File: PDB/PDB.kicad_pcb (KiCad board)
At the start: 2 copper layers, 111.8 x 88.1 mm, 45 parts, among them J1 Conn_01x02, J2 Conn_01x04, Q1 S8050, Sw1 D-SWITCH_MR5-111-C5N-BB, Y1 12MHz

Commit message: Finished board layout?
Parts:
- added ?: , , F.Cu at (92.0, 102.0)
- added ?: , , F.Cu at (151.0, 102.0)
- added ?: , , F.Cu at (93.5, 53.2)
- added ?: , , F.Cu at (151.0, 60.0)
- added C7: 0.1u, Capacitor_SMD:C_0603_1608Metric, F.Cu at (137.2, 70.6)
- added G***: LOGO, PiE_Footprints:PiE Logo, F.Cu at (91.0, 51.5)
- added R17: 22, Resistor_SMD:R_0603_1608Metric, F.Cu at (153.9, 88.5)
- added R18: 22, Resistor_SMD:R_0603_1608Metric, F.Cu at (153.8, 86.5)
- added SW2: SW_SPDT, PiE_Footprints:DEALON SS-12D01-G3, F.Cu at (162.9, 100.9)
- added U3: PCF8574, PiE_Footprints:PCF8574T, F.Cu at (133.3, 76.9)
- Batt1: footprint PiE_Footprints:XT60_F -> PiE_Footprints:AMASS_XT60-M_1x02_P7.20mm_Vertical
- J1: footprint Connector_PinHeader_2.54mm:PinHeader_1x02_P2.54mm_Vertical -> PiE_Footprints:PinHeader_1x02_P2.54mm_Vertical
- J2: footprint Connector_PinHeader_2.54mm:PinHeader_1x04_P2.54mm_Vertical -> PiE_Footprints:PinHeader_1x04_P2.54mm_Vertical
- Jst1: footprint PiE_Footprints:JST_XH_B4B-XH-AM_1x04_P2.50mm_Vertical -> PiE_Footprints:JST_XH_B4B-XH-A_1x04_P2.50mm_Vertical
- Y1: footprint Crystal:Crystal_HC49-U_Vertical -> PiE_Footprints:JYJE S1C12000VWFAC
- moved J2 53.4 mm to (78.5, 101.6), turned to 180 degrees
- moved R1 40.7 mm to (93.6, 95.5), turned to 90 degrees
- moved R2 36.5 mm to (93.6, 92.4), turned to 90 degrees
- moved Pro1 28.2 mm to (104.1, 87.1)
- moved R4 27.2 mm to (93.6, 87.8), turned to 90 degrees
- moved C1 26.2 mm to (122.5, 72.4)
- moved R14 26.0 mm to (137.2, 86.5)
- moved R3 25.9 mm to (93.6, 84.6), turned to -90 degrees
- moved D3 25.4 mm to (130.8, 96.3)
- moved R13 24.3 mm to (127.6, 86.5)
- moved R9 24.3 mm to (122.2, 86.5)
- moved R12 24.3 mm to (126.0, 86.5)
- moved R7 24.3 mm to (118.9, 86.5)
- moved R8 24.3 mm to (120.5, 86.5)
- moved R10 22.1 mm to (138.9, 86.5)
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- renumbered USB4 to DATA1, FTDI1 to U2
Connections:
- DATA1 pad 2: /D- -> Net-(DATA1-Pad2)
- DATA1 pad 3: /D+ -> Net-(DATA1-Pad3)
- Pro1 pad 10: /E -> unconnected-(Pro1-Pad10)
- Pro1 pad 11: /DP -> unconnected-(Pro1-Pad11)
- Pro1 pad 12: /Buzzer -> /Dig4
- Pro1 pad 13: /A -> /Buzzer
- Pro1 pad 14: /F -> /toggle
- Pro1 pad 15: /B -> /Dig3
- Pro1 pad 16: /C -> /Dig2
- Pro1 pad 17: /G -> /Dig1
- Pro1 pad 18: /Cell1_s -> /Cell1+2+3_s
- Pro1 pad 2: /toggle -> /Rx
- Pro1 pad 20: /Cell1+2+3_s -> /Cell1_s
- Pro1 pad 5: /D -> /SDA
- Pro1 pad 6: /Dig4 -> /SCL
- Pro1 pad 7: /Dig2 -> unconnected-(Pro1-Pad7)
- Pro1 pad 8: /Dig3 -> unconnected-(Pro1-Pad8)
- Pro1 pad 9: /Dig1 -> unconnected-(Pro1-Pad9)
- U2 pad 3: unconnected-(FTDI1-Pad3) -> /Rx
- USB1 pad 2: /D- -> unconnected-(USB1-Pad2)
- USB1 pad 3: /D+ -> unconnected-(USB1-Pad3)
- USB2 pad 2: /D- -> unconnected-(USB2-Pad2)
- USB2 pad 3: /D+ -> unconnected-(USB2-Pad3)
- USB3 pad 2: /D- -> unconnected-(USB3-Pad2)
- USB3 pad 3: /D+ -> unconnected-(USB3-Pad3)
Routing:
- net /D-: track 119.8 -> 18.7 mm
- net /toggle: track 0.00 -> 93.3 mm, vias 0 -> 1
- net /D: track 86.7 -> 12.7 mm
- net /Rx: track 0.00 -> 70.8 mm, vias 0 -> 2
- net /D+: track 82.4 -> 18.1 mm
- net /E: track 75.9 -> 15.0 mm, vias 2 -> 0
- net GND: track 150.0 -> 89.8 mm, vias 2 -> 6
- net /Cell1_s: track 63.7 -> 5.85 mm, vias 1 -> 0
- net /Cell1+2_s: track 62.0 -> 5.05 mm, vias 1 -> 0
- net /Cell1: track 69.4 -> 16.2 mm
- net /Cell1+2+3_s: track 60.0 -> 10.1 mm, vias 1 -> 0
- net /5v: track 49.5 -> 1.96 mm, vias 6 -> 0
- net /DP: track 57.9 -> 10.5 mm, vias 1 -> 0
- net /Cell1+2+3: track 72.1 -> 25.1 mm
- net /Buzzer: track 4.23 -> 50.0 mm, vias 0 -> 2
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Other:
- board size 111.8 x 88.1 mm -> 112.1 x 88.3 mm
- board text added: "1"
- board text added: "1+2"
- board text added: "1+2+3"
- board text added: "12v"
- board text added: "12v on"
- board text added: "5v"
- board text added: "Copyright (c) 2023, Pioneers in Engineering All rights reserved. Design by: Justin H This design is open source hardware. For more information, visit github.com/pioneers/PiElectrical"
- board text added: "GND"
- board text added: "Pioneers in Engineering Power Distribution Board"
- board text added: "Pro Micro"

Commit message: ordered this ****
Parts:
- removed ? (x4): , 
- added R19: 4700, Resistor_SMD:R_0603_1608Metric, F.Cu at (132.1, 68.1)
- added R20: 4700, Resistor_SMD:R_0603_1608Metric, F.Cu at (133.8, 68.1)
- added REF**: Hole_R1.62mm, PiE_Footprints:Hole_R1.62mm, F.Cu at (92.0, 60.0)
- added REF**: Hole_R1.62mm, PiE_Footprints:Hole_R1.62mm, F.Cu at (92.0, 102.0)
- added REF**: Hole_R1.62mm, PiE_Footprints:Hole_R1.62mm, F.Cu at (81.7, 36.7)
- added REF**: Hole_R1.62mm, PiE_Footprints:Hole_R1.62mm, F.Cu at (151.1, 102.0)
- added REF**: Hole_R1.62mm, PiE_Footprints:Hole_R1.62mm, F.Cu at (151.0, 59.9)
- moved Converter1 3.08 mm to (118.3, 23.7)
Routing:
- net /battery: track 28.6 -> 0.00 mm
- net /5v: track 1.96 -> 20.4 mm, vias 0 -> 2
- net /fuse out: track 54.2 -> 70.3 mm
- net /SCL: track 36.7 -> 44.3 mm
- net /SDA: track 36.4 -> 42.0 mm
- net /Buzzer: track 50.0 -> 55.3 mm
- net GND: track 89.8 -> 88.5 mm
- net /E: track 15.0 -> 14.0 mm
- added copper zone on F.Cu, net /battery

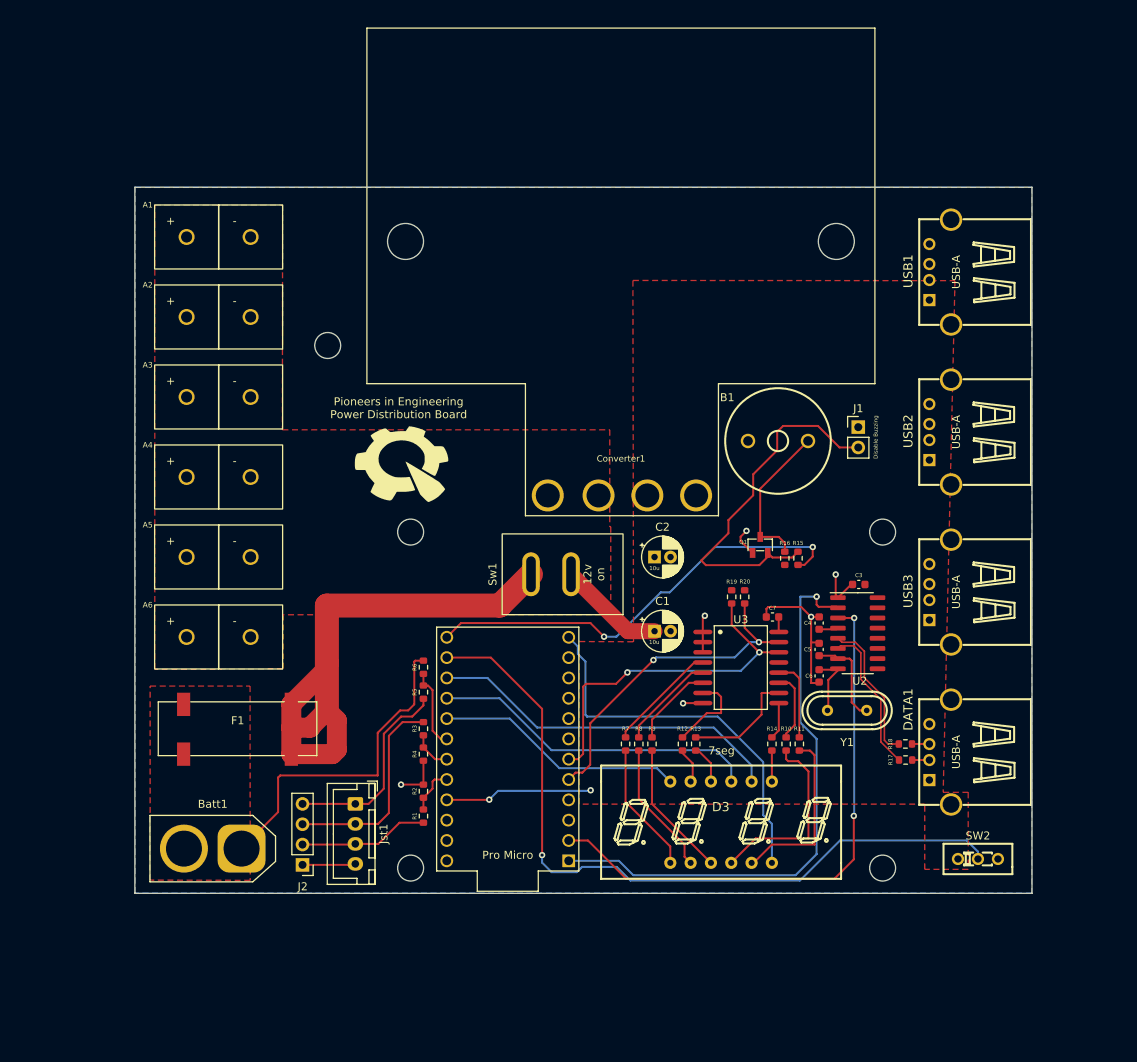
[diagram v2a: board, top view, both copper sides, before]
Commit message: fixed PDB layout
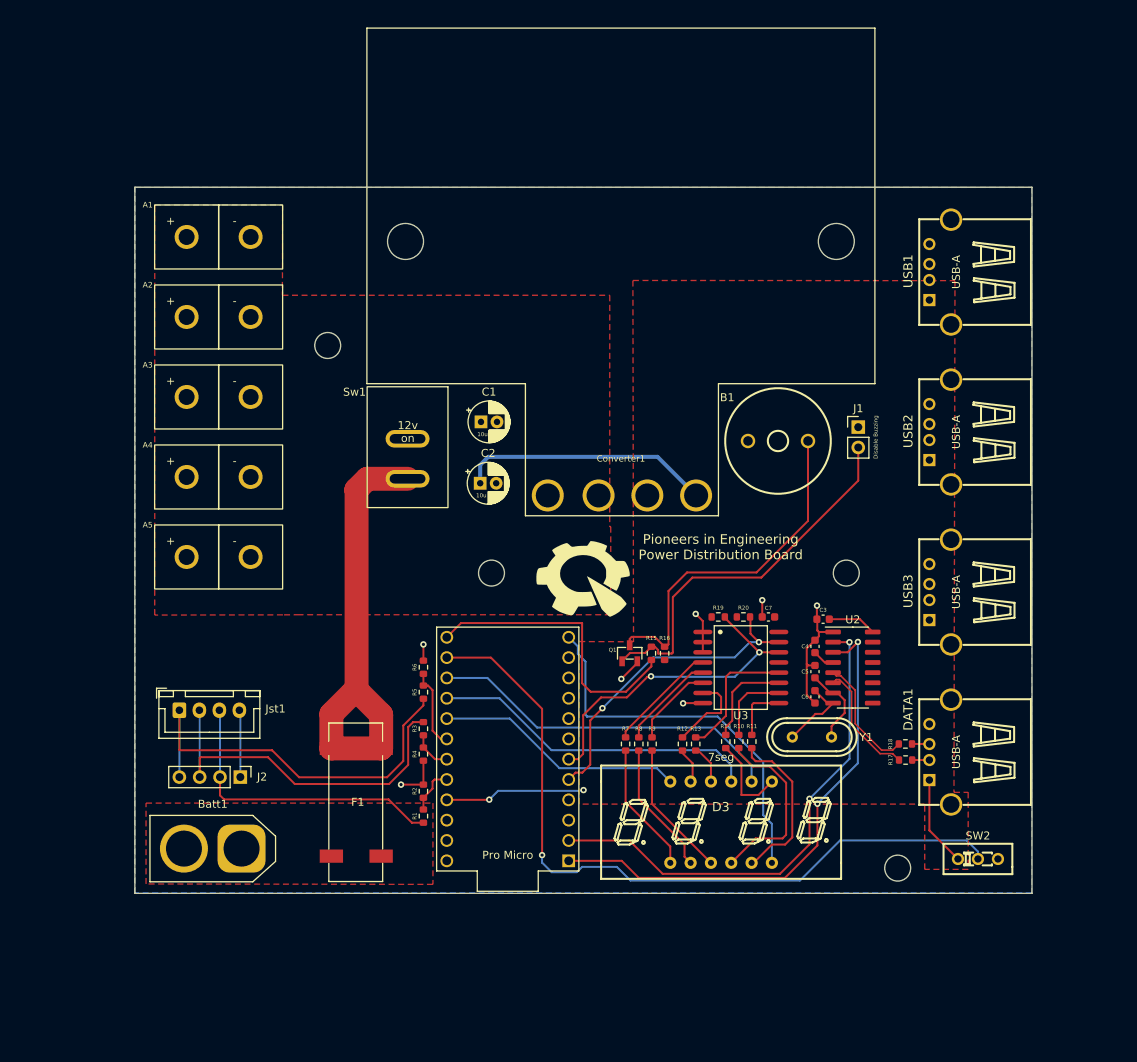
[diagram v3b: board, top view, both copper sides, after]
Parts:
- removed A6: Anderson_Horizontal, PiE_Footprints:anderson_horizontal
- removed the REF** at (92.0, 102.0)
- Converter1: value 5v_converter -> BUCK_CONVERTER_5V
- Q1: value S8050 -> s8050_JSMSEMI; footprint PiE_Footprints:s8050 SMD -> PiE_Footprints:s8050 JSMSEMI
- U2: footprint Package_SO:SOIC-16_3.9x9.9mm_P1.27mm -> PiE_Footprints:CH340g
- moved C1 34.0 mm to (100.8, 46.2)
- moved G*** 26.8 mm to (113.7, 65.8)
- moved Jst1 24.9 mm to (63.1, 82.3), turned to 0 degrees
- moved C2 23.7 mm to (100.7, 53.9)
- moved R15 21.8 mm to (122.1, 75.2)
- moved Q1 21.8 mm to (120.3, 77.0)
- moved Sw1 19.5 mm to (91.6, 53.3), turned to 90 degrees
- moved R16 19.2 mm to (123.7, 75.2)
- moved F1 17.4 mm to (85.1, 93.8), turned to 90 degrees
- moved J2 13.4 mm to (70.7, 90.6), turned to -90 degrees
- moved REF** 11.4 mm to (102.2, 65.1)
- moved C3 6.22 mm to (143.6, 70.9)
- moved R11 5.95 mm to (134.6, 86.2)
- moved R10 5.93 mm to (133.0, 86.2)
- moved R14 5.77 mm to (131.4, 86.2)
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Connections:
- net Net-(B1-Pad2) renamed /collector
- J1 pad 2: Net-(J1-Pad2) -> /base
- Q1 pad 1: GND -> /base
- Q1 pad 2: Net-(J1-Pad2) -> GND
- R15 pad 2: Net-(J1-Pad2) -> /base
- U2 pad 2: /Tx -> /Rx
- U2 pad 3: /Rx -> /Tx
- U3 pad 10: /F -> /C
- U3 pad 11: /C -> /B
- U3 pad 12: /G -> /F
- U3 pad 9: /B -> /G
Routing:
- net /base: track 0.00 -> 48.1 mm
- net /5v: track 20.4 -> 66.7 mm
- net Net-(J1-Pad2): track 45.4 -> 0.00 mm
- net GND: track 88.5 -> 45.2 mm, vias 6 -> 7
- net /Cell1+2+3: track 25.1 -> 52.4 mm
- net /collector: track 18.9 -> 44.1 mm
- net /Cell1: track 16.2 -> 37.5 mm
- net /Cell1+2: track 26.1 -> 46.1 mm
- net /Buzzer: track 55.3 -> 36.4 mm, vias 2 -> 0
- net /fuse out: track 70.3 -> 55.6 mm
- net /12v: track 13.4 -> 0.00 mm
- net /Rx: track 70.8 -> 62.7 mm
- net /B: track 4.64 -> 12.0 mm
- net Net-(D3-Pad7): track 3.87 -> 11.2 mm
- net /Tx: track 71.7 -> 64.8 mm, vias 1 -> 2
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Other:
- board text added: "Copyright (c) 2023, Pioneers in Engineering All rights reserved. Design by: Justin H With help from: Ricky L This design is open source hardware. For more information, visit github.com/pioneers/PiElectrical"
- board text removed: "Copyright (c) 2023, Pioneers in Engineering All rights reserved. Design by: Justin H This design is open source hardware. For more information, visit github.com/pioneers/PiElectrical"
